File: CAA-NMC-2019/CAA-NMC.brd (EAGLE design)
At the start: 33.3 x 100 mm, 157 parts, among them IC1 ATTINY85-20SU, J1 M20-9980346

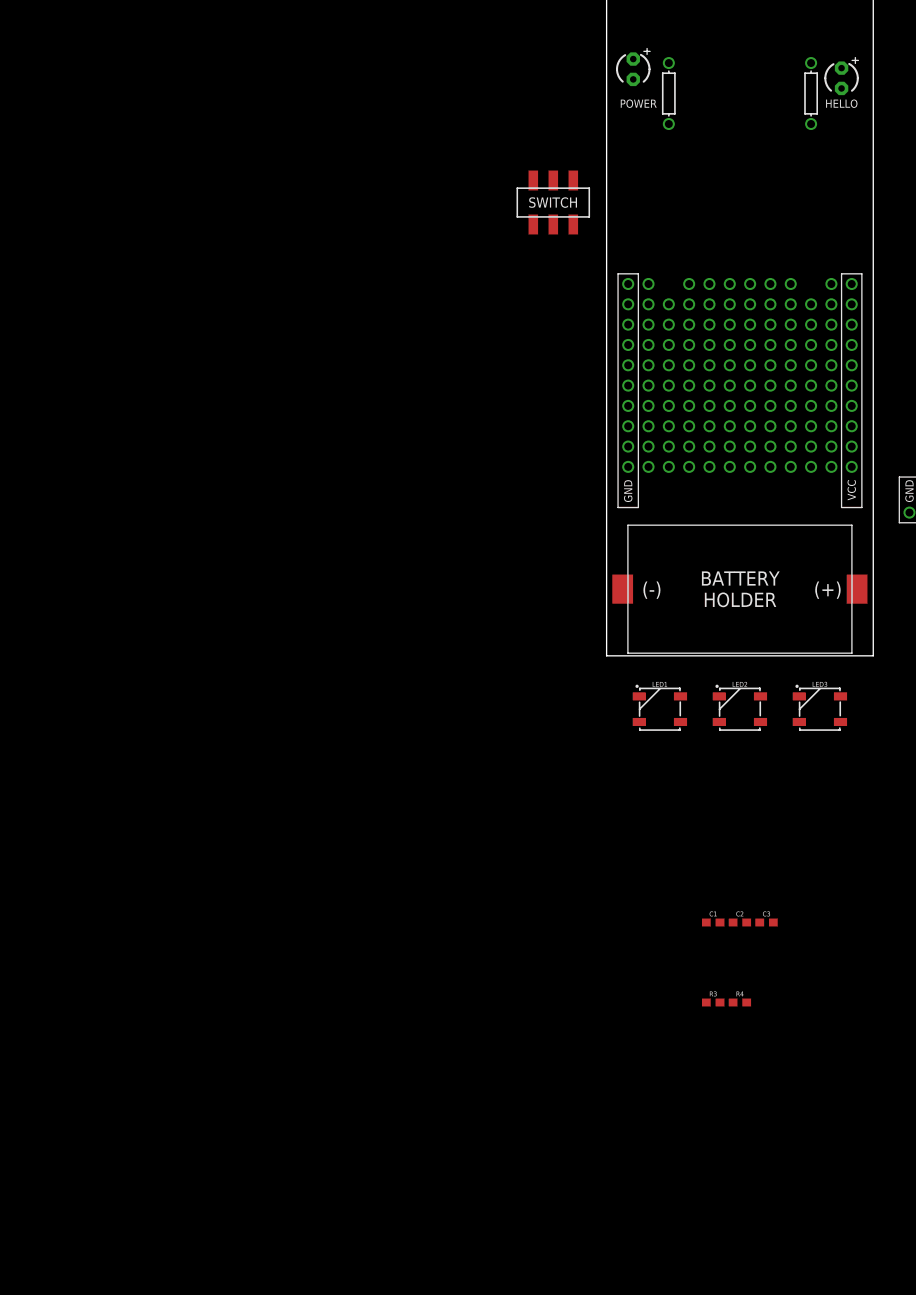
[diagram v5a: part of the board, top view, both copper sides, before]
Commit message: updated lbr, proto area simplified
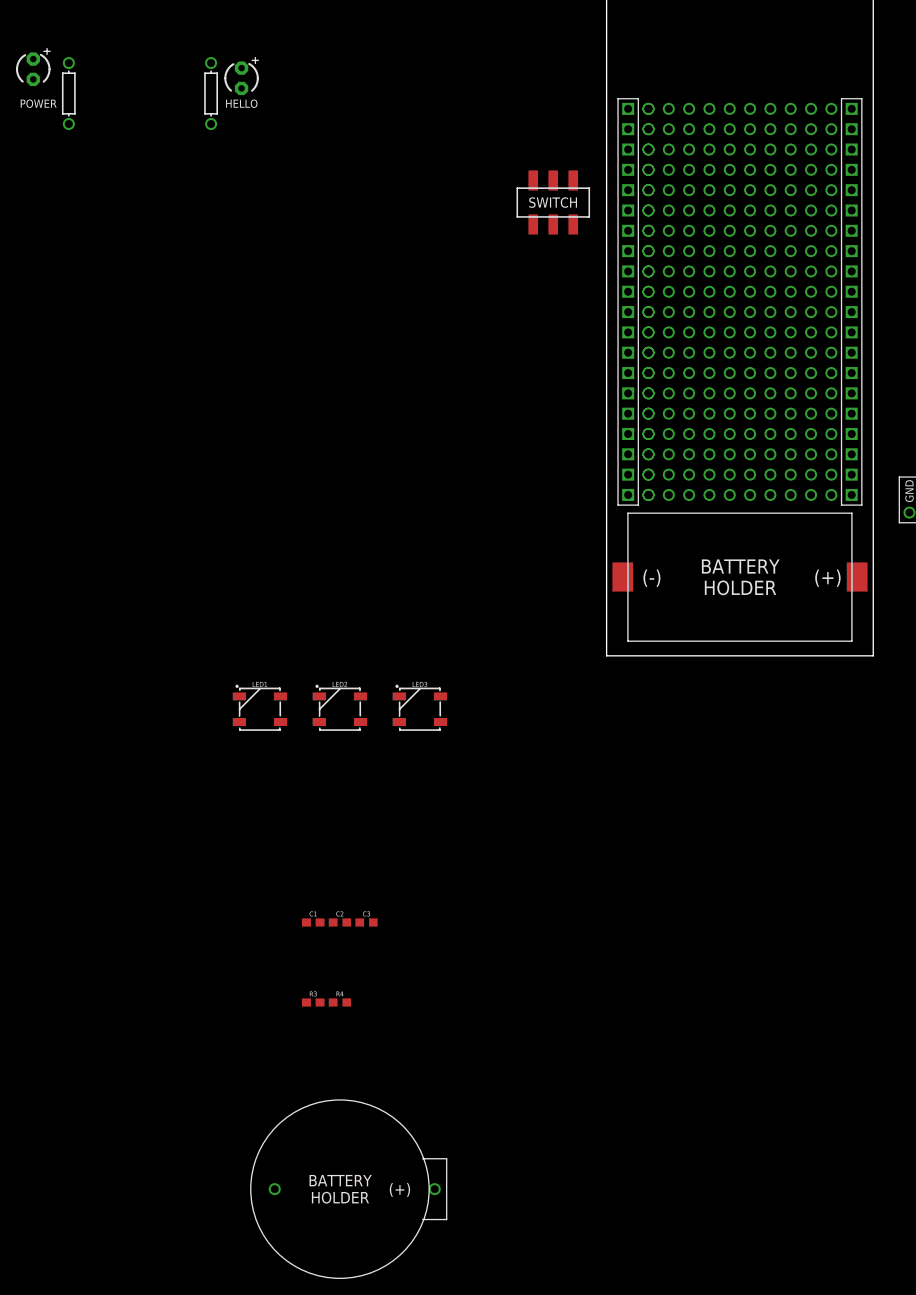
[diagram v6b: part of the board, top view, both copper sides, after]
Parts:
- removed U$10, U$100, U$101, U$102, U$103, U$104, U$105, U$106, U$107, U$108, U$109, U$11, U$110, U$111, U$112, U$113, U$114, U$115, U$116, U$117, U$118, U$119, U$12, U$120, U$121, U$122, U$124, U$125, U$128, U$129, U$13, U$130, U$131, U$132, U$133, U$134, U$135, U$136, U$137, U$138, U$139, U$14, U$140, U$141, U$142, U$143, U$15, U$16, U$17, U$18, U$19, U$20, U$21, U$22, U$23, U$24, U$25, U$26, U$27, U$28, U$29, U$3, U$30, U$31, U$32, U$33, U$34, U$35, U$36, U$37, U$38, U$39, U$4, U$40, U$41, U$42, U$43, U$44, U$45, U$46, U$47, U$48, U$49, U$5, U$50, U$51, U$52, U$53, U$54, U$55, U$56, U$57, U$58, U$59, U$6, U$60, U$61, U$62, U$63, U$64, U$65, U$66, U$67, U$68, U$69, U$7, U$70, U$8, U$9, U$93, U$94, U$95, U$96, U$97, U$98, U$99: ONE_PAD, BadgeParts:1X01
- U$1: value ONE_PAD -> PROTO; device BadgeParts:1X01 -> BadgeParts:PROTO
- U$2: value ONE_PAD -> THRU-CR-HOLDER; device BadgeParts:1X01 -> BadgeParts:THRU-CR-HOLDER
- moved U$2 112.4 mm to (-33.3, -66.7)
- moved HELLO 75.0 mm to (-45.6, 72.2)
- moved POWER 75.0 mm to (-71.7, 73.3)
- moved U$126 75.0 mm to (-67.2, 70.3)
- moved U$127 75.0 mm to (-49.4, 70.3)
- moved C1 50.0 mm to (-36.7, -33.3)
- moved C2 50.0 mm to (-33.3, -33.3)
- moved C3 50.0 mm to (-30.0, -33.3)
- moved LED1 50.0 mm to (-43.3, -6.67)
- moved LED2 50.0 mm to (-33.3, -6.67)
- moved LED3 50.0 mm to (-23.3, -6.67)
- moved R3 50.0 mm to (-36.7, -43.3)
- moved R4 50.0 mm to (-33.3, -43.3)
- moved U$1 14.2 mm to (16.7, 20.1)
- moved U$144 1.50 mm to (16.7, 9.83)
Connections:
- net GND: no longer U$100.P$1, U$124.P$1, U$125.P$1, U$128.P$1, U$129.P$1, U$130.P$1, U$131.P$1, U$132.P$1, U$133.P$1, U$99.P$1
- net VCC: no longer U$134.P$1, U$135.P$1, U$136.P$1, U$137.P$1, U$138.P$1, U$139.P$1, U$140.P$1, U$141.P$1, U$142.P$1, U$143.P$1

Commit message: lbr updates, proto area con't
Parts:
- moved U$2 91.0 mm to (16.7, 9.34)
- moved U$144 0.49 mm to (16.7, 9.34)
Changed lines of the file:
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@@
 <element name="U$126" library="BadgeParts" package="AXIAL-0.3" value="RESISTOR" x="-67.22" y="70.29" smashed="yes" rot="R270"/>
 <element name="U$127" library="BadgeParts" package="AXIAL-0.3" value="RESISTOR" x="-49.44" y="70.29" smashed="yes" rot="R270"/>
-<element name="U$144" library="BadgeParts" package="SMT-CR-HOLDER" value="SMT-BATTERY-HOLDER" x="16.666" y="9.833" smashed="yes" rot="R180"/>
+<element name="U$144" library="BadgeParts" package="SMT-CR-HOLDER" value="SMT-BATTERY-HOLDER" x="16.666" y="9.3415" smashed="yes" rot="R180"/>
 <element name="LED1" library="SparkFun-LED" library_urn="urn:adsk.eagle:library:529" package="WS2812B" package3d_urn="urn:adsk.eagle:package:39369/1" value="WS2812B" x="-43.334" y="-6.666" smashed="yes">
 <attribute name="NAME" x="-43.334" y="-3.872" size="0.6096" layer="25" font="vector" ratio="20" align="bottom-center"/>
@@
 <element name="U$145" library="BadgeParts" package="SMT-SWITCH" value="SMT-SWITCH" x="-6.666" y="56.661" smashed="yes"/>
 <element name="U$1" library="BadgeParts" package="PROTO" value="PROTO" x="16.666" y="20.1103" smashed="yes"/>
-<element name="U$2" library="BadgeParts" package="THRU-CR-HOLDER" value="THRU-CR-HOLDER" x="-33.332" y="-66.664" smashed="yes"/>
+<element name="U$2" library="BadgeParts" package="THRU-CR-HOLDER" value="THRU-CR-HOLDER" x="16.666" y="9.3415" smashed="yes"/>
 </elements>
 <signals>
@@
 <wire x1="-67.22" y1="66.48" x2="8.415" y2="93.815" width="0" layer="19" extent="1-1"/>
 <wire x1="45.48" y1="17.905" x2="-67.22" y2="66.48" width="0" layer="19" extent="1-1"/>
-<wire x1="31.316" y1="9.833" x2="45.48" y2="17.905" width="0" layer="19" extent="1-1"/>
+<wire x1="31.316" y1="9.3415" x2="45.48" y2="17.905" width="0" layer="19" extent="1-1"/>
 </signal>
 <signal name="PB3">
@@
 <wire x1="-35.912" y1="-5.066" x2="-25.913" y2="-5.066" width="0" layer="19" extent="1-1"/>
 <wire x1="-45.911" y1="-5.066" x2="-35.912" y2="-5.066" width="0" layer="19" extent="1-1"/>
-<wire x1="2.016" y1="9.833" x2="-45.911" y2="-5.066" width="0" layer="19" extent="1-1"/>
+<wire x1="2.016" y1="9.3415" x2="-45.911" y2="-5.066" width="0" layer="19" extent="1-1"/>
 <wire x1="-35.818" y1="-33.33" x2="-35.912" y2="-5.066" width="0" layer="19" extent="1-1"/>
 <wire x1="-32.485" y1="-33.33" x2="-35.818" y2="-33.33" width="0" layer="19" extent="1-1"/>

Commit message: recentered origin
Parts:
- moved C3 100.0 mm to (-130.0, -33.3)
- moved C1 100.0 mm to (-136.7, -33.3)
- moved C2 100.0 mm to (-133.3, -33.3)
- moved HELLO 100.0 mm to (-145.6, 72.2)
- moved LED1 100.0 mm to (-143.3, -6.67)
- moved LED2 100.0 mm to (-133.3, -6.67)
- moved LED3 100.0 mm to (-123.3, -6.67)
- moved POWER 100.0 mm to (-171.7, 73.3)
- moved R3 100.0 mm to (-136.7, -43.3)
- moved R4 100.0 mm to (-133.3, -43.3)
- moved U$126 100.0 mm to (-167.2, 70.3)
- moved U$127 100.0 mm to (-149.4, 70.3)
- moved U$145 74.9 mm to (63.6, 82.6)
- moved J1 39.3 mm to (45.2, 92.9)
- moved U$1 17.4 mm to (0.00, 25.0)
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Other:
- outline, holes or cut-outs redrawn
